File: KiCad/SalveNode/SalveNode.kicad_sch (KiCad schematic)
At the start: 22 parts, among them IC2 TMP75AQDGKRQ1, IC3 DS89C21TMX_NOPB, IC3 VEML7700-TR, J1 AVR-ISP-6, J2 691382040006, U1 MCP1700x-330xxTT, U2 ATmega328PB-A, Y1 16M

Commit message: Production
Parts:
- removed J2: 691382040006, SimbolosSnapEDA:691382040006, symbol 691382040006:691382040006
- added J3: 691382030006, SimbolosSnapEDA:691382030006, symbol 691382030006:691382030006
- C1, C9: Mouser Part Number (none) -> C1206X105K1RACAUTO
- J1: footprint Connector_PinHeader_1.00mm:PinHeader_2x03_P1.00mm_Vertical -> Connector_PinHeader_2.54mm:PinHeader_2x03_P2.54mm_Vertical
- R7: value PAD -> 50
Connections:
- net +5V: now also J3.1
- net D0+: now also J3.3
- net D0-: now also J3.2
- net Earth: now also J3.6
- net RI+: now also J3.5
- net RI-: now also J3.4
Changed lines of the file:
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@@
       (effects (font (size 1.27 1.27)) (justify right))
     )
-    (property "Footprint" "Connector_PinHeader_1.00mm:PinHeader_2x03_P1.00mm_Vertical" (at 17.78 85.09 90)
+    (property "Footprint" "Connector_PinHeader_2.54mm:PinHeader_2x03_P2.54mm_Vertical" (at 17.78 85.09 90)
       (effects (font (size 1.27 1.27)) hide)
     )
@@
       (effects (font (size 1.27 1.27)) hide)
     )
-    (property "Mouser Part Number" "" (at 20.32 146.05 0)
+    (property "Mouser Part Number" "C1206X105K1RACAUTO" (at 20.32 146.05 0)
       (effects (font (size 1.27 1.27)) hide)
     )
@@
     )
   )
-  (symbol (lib_id "691382040006:691382040006") (at 25.4 22.86 0) (unit 1)
-    (in_bom yes) (on_board yes) (dnp no) (fields_autoplaced)
-    (property "Reference" "J2" (at 26.67 17.78 0)
-      (effects (font (size 1.27 1.27)))
-    )
-    (property "Value" "691382040006" (at 26.67 20.32 0)
-      (effects (font (size 1.27 1.27)))
-    )
-    (property "Footprint" "SimbolosSnapEDA:691382040006" (at 25.4 22.86 0)
+  (symbol (lib_name "+5V_1") (lib_id "power:+5V") (at 20.32 53.34 0) (unit 1)
+    (in_bom yes) (on_board yes) (dnp no) (fields_autoplaced)
+    (property "Reference" "#PWR0123" (at 20.32 57.15 0)
+      (effects (font (size 1.27 1.27)) hide)
+    )
+    (property "Value" "+5V" (at 20.32 48.26 0)
+      (effects (font (size 1.27 1.27)))
+    )
+    (property "Footprint" "" (at 20.32 53.34 0)
+      (effects (font (size 1.27 1.27)) hide)
+    )
+    (property "Datasheet" "" (at 20.32 53.34 0)
+      (effects (font (size 1.27 1.27)) hide)
+    )
+    (pin "1")
+    (instances
+      (project "KiCad"
+        (path "/557850ac-a946-4dff-8187-8978353577df"
+          (reference "#PWR0123") (unit 1)
+        )
+      )
+      (project "SalveNode"
+        (path "/947c7390-073c-40c7-ae18-83309c4a488f"
+          (reference "#PWR03") (unit 1)
+        )
+      )
+    )
+  )
+  (symbol (lib_id "691382030006:691382030006") (at 25.4 22.86 0) (unit 1)
+    (in_bom yes) (on_board yes) (dnp no) (fields_autoplaced)
+    (property "Reference" "J3" (at 26.67 17.78 0)
+      (effects (font (size 1.27 1.27)))
+    )
+    (property "Value" "691382030006" (at 26.67 20.32 0)
+      (effects (font (size 1.27 1.27)))
+    )
+    (property "Footprint" "SimbolosSnapEDA:691382030006" (at 25.4 22.86 0)
       (effects (font (size 1.27 1.27)) (justify bottom) hide)
     )
@@
       (effects (font (size 1.27 1.27)) hide)
     )
-    (property "DigiKey_Part_Number" "732-6047-ND" (at 25.4 22.86 0)
-      (effects (font (size 1.27 1.27)) (justify bottom) hide)
-    )
-    (property "SnapEDA_Link" "https://www.snapeda.com/parts/691382040006/Wurth+Elektronik/view-part/?ref=snap" (at 25.4 22.86 0)
-      (effects (font (size 1.27 1.27)) (justify bottom) hide)
-    )
-    (property "Description" "\n6 Position Terminal Block Header, Male Pins, Shrouded (4 Side) 0.098 (2.50mm) 90°, Right Angle Through Hole\n" (at 25.4 22.86 0)
+    (property "DigiKey_Part_Number" "" (at 25.4 22.86 0)
+      (effects (font (size 1.27 1.27)) (justify bottom) hide)
+    )
+    (property "MF" "Wurth Electronics" (at 25.4 22.86 0)
+      (effects (font (size 1.27 1.27)) (justify bottom) hide)
+    )
+    (property "Purchase-URL" "https://www.snapeda.com/api/url_track_click_mouser/?unipart_id=1195359&manufacturer=Wurth Electronics&part_name=691382030006&search_term=691382030006" (at 25.4 22.86 0)
       (effects (font (size 1.27 1.27)) (justify bottom) hide)
     )
@@
       (effects (font (size 1.27 1.27)) (justify bottom) hide)
     )
-    (property "VALUE" "691382040006" (at 25.4 22.86 0)
+    (property "VALUE" "691382030006" (at 25.4 22.86 0)
       (effects (font (size 1.27 1.27)) (justify bottom) hide)
     )
@@
       (effects (font (size 1.27 1.27)) (justify bottom) hide)
     )
-    (property "MF" "Wurth Elektronik" (at 25.4 22.86 0)
-      (effects (font (size 1.27 1.27)) (justify bottom) hide)
-    )
-    (property "DATASHEET-URL" "https://www.we-online.com/redexpert/spec/691382040006?ae" (at 25.4 22.86 0)
-      (effects (font (size 1.27 1.27)) (justify bottom) hide)
-    )
-    (property "MP" "691382040006" (at 25.4 22.86 0)
+    (property "SnapEDA_Link" "https://www.snapeda.com/parts/691382030006/Wurth+Electronics+Inc./view-part/?ref=snap" (at 25.4 22.86 0)
+      (effects (font (size 1.27 1.27)) (justify bottom) hide)
+    )
+    (property "DATASHEET-URL" "https://www.we-online.com/redexpert/spec/691382030006?ae" (at 25.4 22.86 0)
+      (effects (font (size 1.27 1.27)) (justify bottom) hide)
+    )
+    (property "MP" "691382030006" (at 25.4 22.86 0)
       (effects (font (size 1.27 1.27)) (justify bottom) hide)
     )
@@
       (effects (font (size 1.27 1.27)) (justify bottom) hide)
     )
-    (property "PART-NUMBER" "691382040006" (at 25.4 22.86 0)
-      (effects (font (size 1.27 1.27)) (justify bottom) hide)
-    )
-    (property "TYPE" "Horizontal" (at 25.4 22.86 0)
-      (effects (font (size 1.27 1.27)) (justify bottom) hide)
-    )
-    (property "Check_prices" "https://www.snapeda.com/parts/691382040006/Wurth+Elektronik/view-part/?ref=eda" (at 25.4 22.86 0)
-      (effects (font (size 1.27 1.27)) (justify bottom) hide)
-    )
-    (property "Mouser Part Number" "691382040006" (at 25.4 22.86 0)
-      (effects (font (size 1.27 1.27)) hide)
+    (property "PART-NUMBER" "691382030006" (at 25.4 22.86 0)
+      (effects (font (size 1.27 1.27)) (justify bottom) hide)
+    )
+    (property "Description" "\n6 Position Terminal Block Header, Male Pins, Shrouded (4 Side) 0.098 (2.50mm) Vertical Through Hole\n" (at 25.4 22.86 0)
+      (effects (font (size 1.27 1.27)) (justify bottom) hide)
+    )
+    (property "TYPE" "Vertical" (at 25.4 22.86 0)
+      (effects (font (size 1.27 1.27)) (justify bottom) hide)
+    )
+    (property "Check_prices" "https://www.snapeda.com/parts/691382030006/Wurth+Electronics+Inc./view-part/?ref=eda" (at 25.4 22.86 0)
+      (effects (font (size 1.27 1.27)) (justify bottom) hide)
     )
     (pin "1")
@@
       (project "SalveNode"
         (path "/947c7390-073c-40c7-ae18-83309c4a488f"
-          (reference "J2") (unit 1)
-        )
-      )
-    )
-  )
-  (symbol (lib_name "+5V_1") (lib_id "power:+5V") (at 20.32 53.34 0) (unit 1)
-    (in_bom yes) (on_board yes) (dnp no) (fields_autoplaced)
-    (property "Reference" "#PWR0123" (at 20.32 57.15 0)
-      (effects (font (size 1.27 1.27)) hide)
-    )
-    (property "Value" "+5V" (at 20.32 48.26 0)
-      (effects (font (size 1.27 1.27)))
-    )
-    (property "Footprint" "" (at 20.32 53.34 0)
-      (effects (font (size 1.27 1.27)) hide)
-    )
-    (property "Datasheet" "" (at 20.32 53.34 0)
-      (effects (font (size 1.27 1.27)) hide)
-    )
-    (pin "1")
-    (instances
-      (project "KiCad"
-        (path "/557850ac-a946-4dff-8187-8978353577df"
-          (reference "#PWR0123") (unit 1)
-        )
-      )
-      (project "SalveNode"
-        (path "/947c7390-073c-40c7-ae18-83309c4a488f"
-          (reference "#PWR03") (unit 1)
+          (reference "J3") (unit 1)
         )
       )
@@
       (effects (font (size 1.27 1.27)) (justify right))
     )
-    (property "Value" "PAD" (at 63.5 55.88 0)
+    (property "Value" "50" (at 63.5 55.88 0)
       (effects (font (size 1.27 1.27)) (justify right))
     )
@@
       (effects (font (size 1.27 1.27)) hide)
     )
-    (property "Mouser Part Number" "" (at 44.45 146.05 0)
-      (effects (font (size 1.27 1.27)) hide)
-    )
+    (property "Mouser Part Number" "C1206X105K1RACAUTO" (at 44.45 146.05 0)
+      (effects (font (size 1.27 1.27)) hide)
+    )

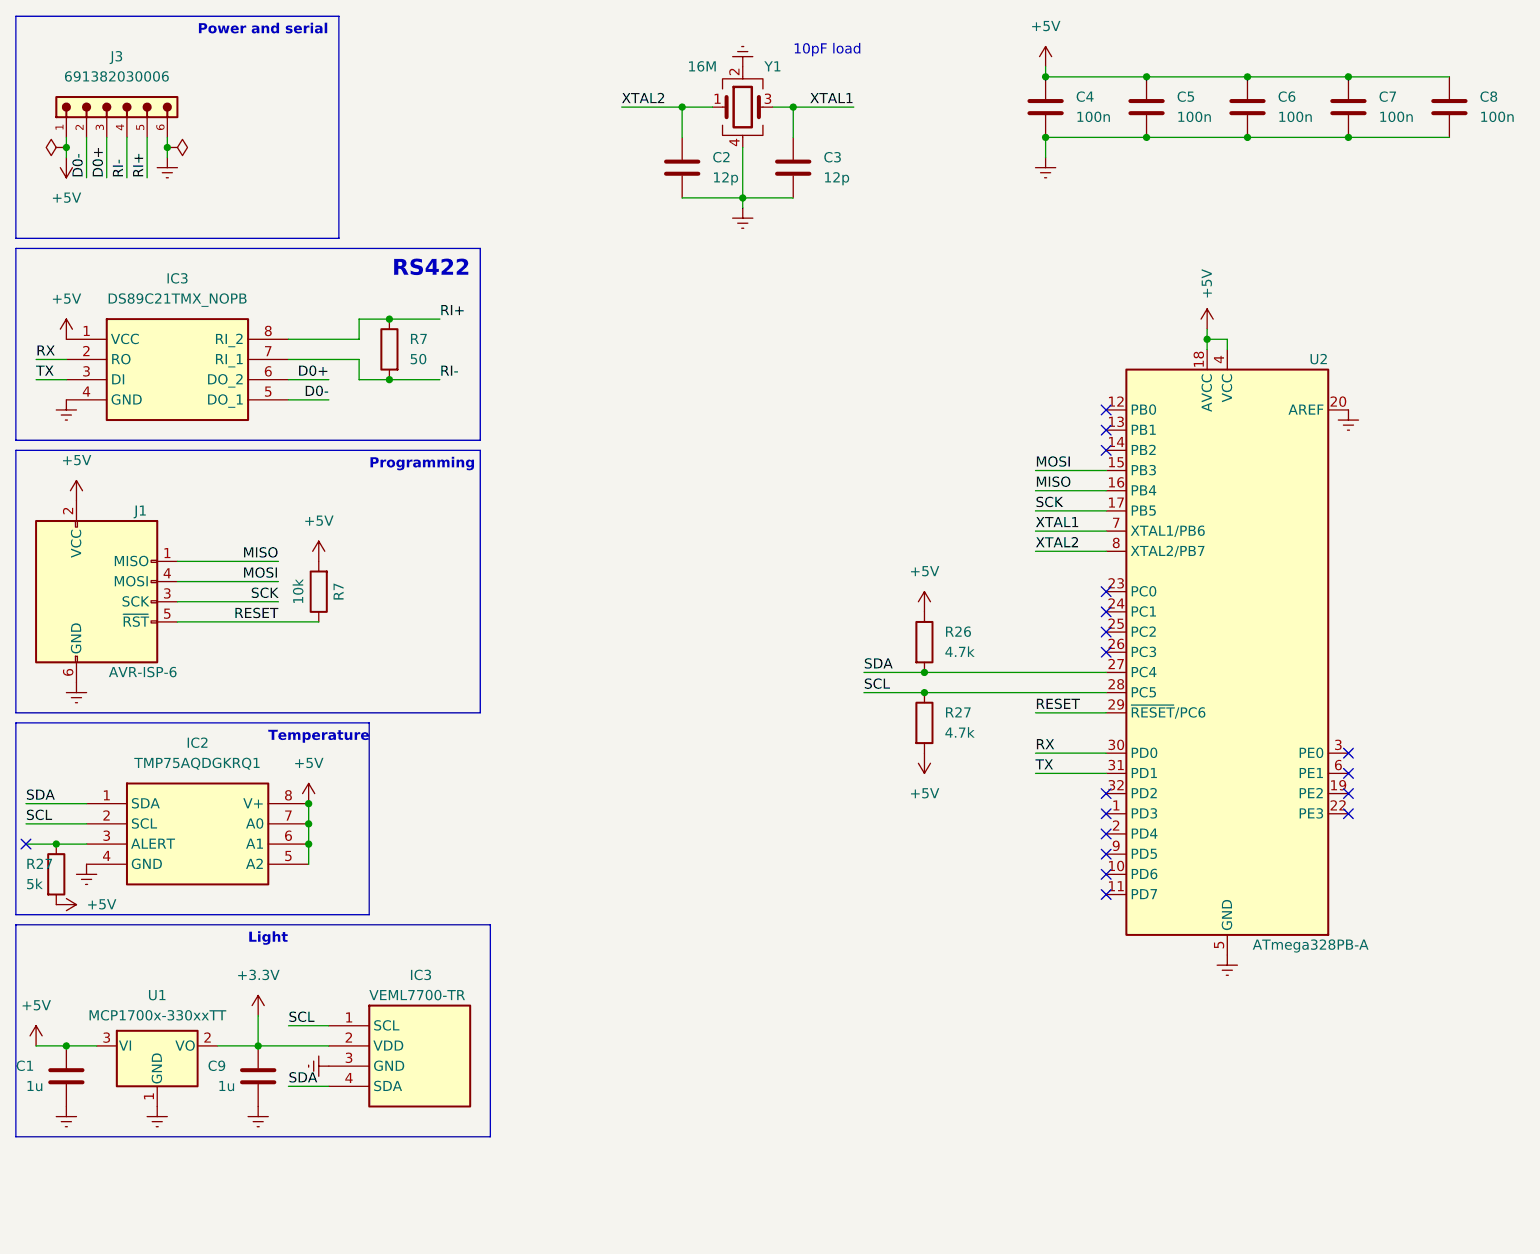
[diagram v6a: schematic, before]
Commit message: modified schematics and continued development of Arduino programs
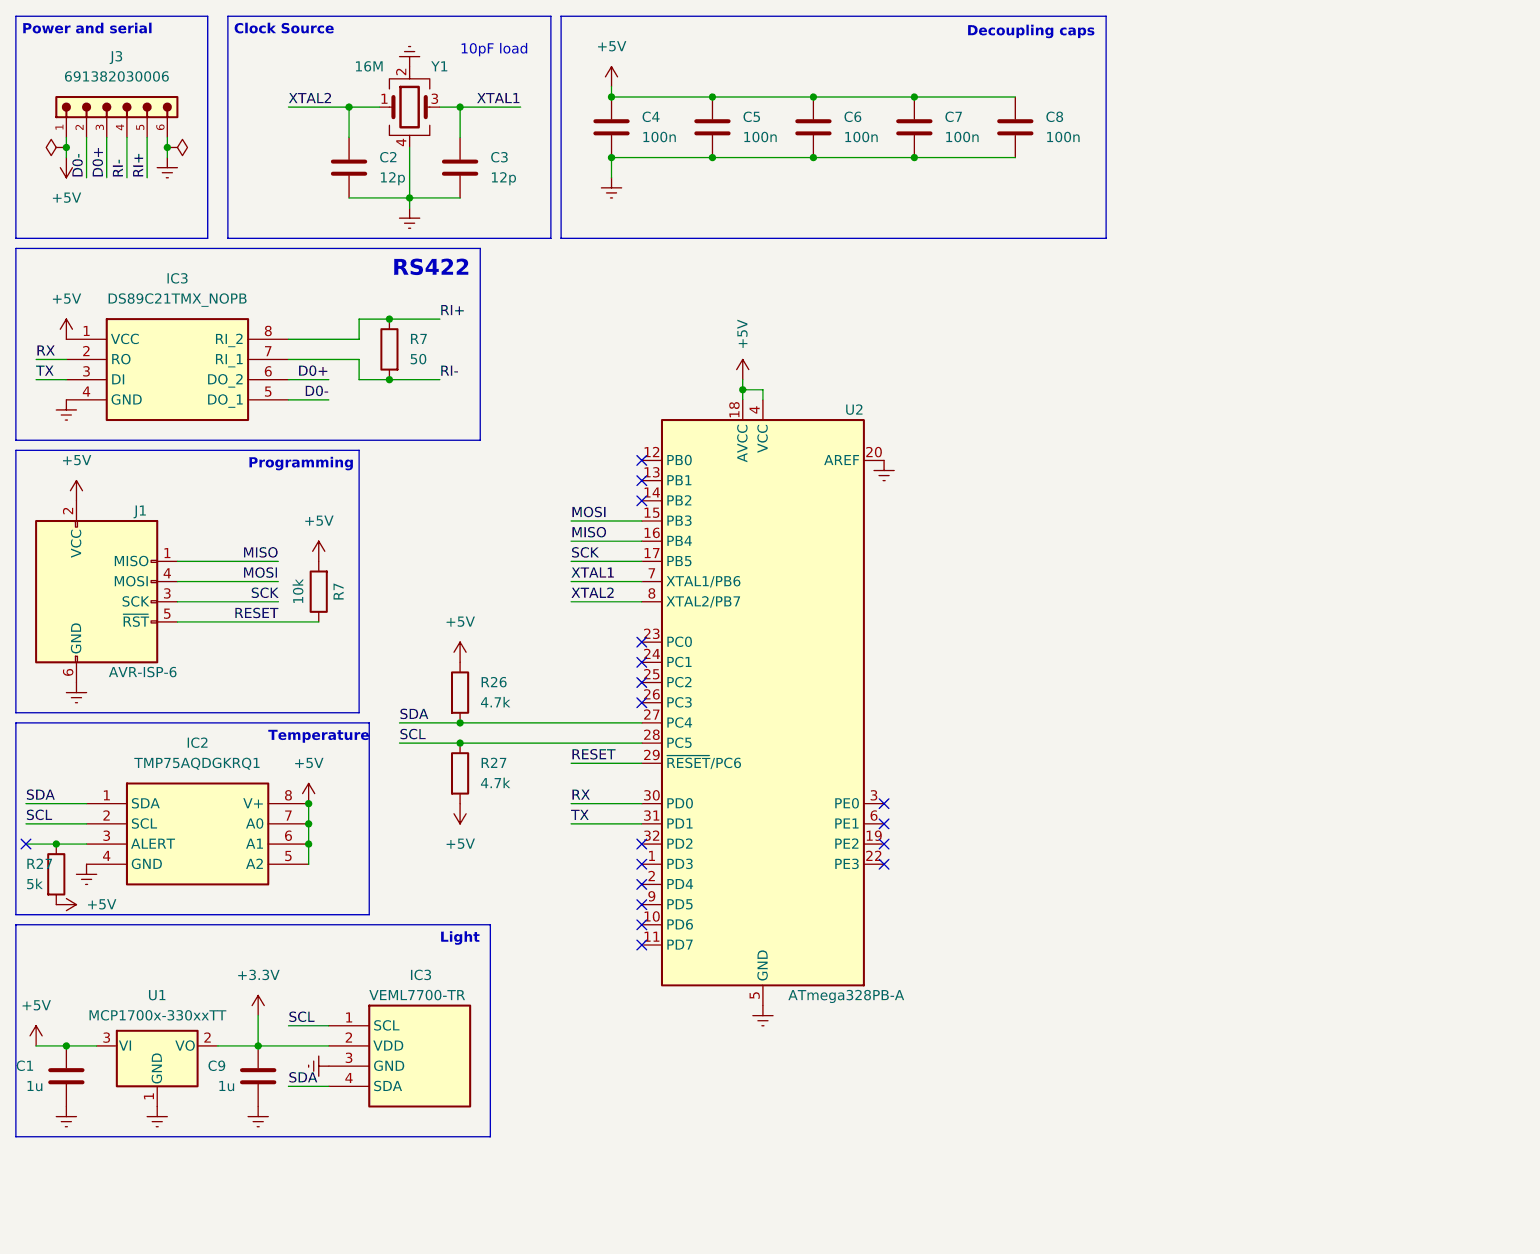
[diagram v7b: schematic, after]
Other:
- note added: "Clock Source"
- note added: "Decoupling caps"
- moved on the sheet: C2, C3, C4, C5, C6, C7, C8, R26, R27, U2, Y1
